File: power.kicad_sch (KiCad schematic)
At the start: 0 parts

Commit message: started on power
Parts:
- added C129, C131: 10n, Capacitor_SMD:C_0402_1005Metric, symbol Auto_Library_WUT:Kemet C0402C103K4PACTU
- added C130, C132: 10u, Capacitor_SMD:C_1206_3216Metric, symbol Auto_Library_WUT:Kyocera AVX 1206DD106MAT2A
- added C133, C134: 220p, Capacitor_SMD:C_0402_1005Metric, symbol Auto_Library_WUT:Kemet C0402C221G5GACTU
- added C135: 100n, Capacitor_SMD:C_0402_1005Metric, symbol Auto_Library_WUT:Yageo CC0402KRX7R8BB104
- added C136: 1u, Capacitor_SMD:C_0402_1005Metric, symbol Auto_Library_WUT:Kemet C0402C105K4PACTU
- added C137, C138, C141, C142: 47u, Capacitor_SMD:C_1206_3216Metric, symbol Auto_Library_WUT:TDK C3216X5R1E476M160AC
- added C139, C140: 10p, Capacitor_SMD:C_0402_1005Metric, symbol Auto_Library_WUT:Kemet C0402C100D4GACTU
- added L2, L3: 2u2, Inductor_WUT:Coilcraft_XEL4030, symbol Auto_Library_WUT:Coilcraft XEL4030-222MED
- added R64, R69, R71: 15k, Resistor_SMD:R_0402_1005Metric, symbol Auto_Library_WUT:KOA Speer RK73H1ETTP1502F
- added R65: 120k, Resistor_SMD:R_0402_1005Metric, symbol Auto_Library_WUT:KOA Speer RK73H1ETTP1203F
- added R66, R67: 10k, Resistor_SMD:R_0402_1005Metric, symbol Auto_Library_WUT:KOA Speer RK73H1ETTP1002F
- added R68, R70: 0R0, Resistor_SMD:R_0402_1005Metric, symbol Auto_Library_WUT:KOA Speer RK73Z1ETTP
- added R73: 300k, Resistor_SMD:R_0402_1005Metric, symbol Auto_Library_WUT:KOA Speer RK73H1ETTP3003F
- added R74: 56k, Resistor_SMD:R_0402_1005Metric, symbol Auto_Library_WUT:KOA Speer RK73H1ETTP5602F
- added R75: 470k, Resistor_SMD:R_0402_1005Metric, symbol Auto_Library_WUT:KOA Speer RK73H1ETTP4703F
- added R76: 150k, Resistor_SMD:R_0402_1005Metric, symbol Auto_Library_WUT:KOA Speer RK73H1ETTP1503F
- added R77: 100k, Resistor_SMD:R_0402_1005Metric, symbol Auto_Library_WUT:KOA Speer RK73H1ETTP1003F
- added R78, R79: 56m, Resistor_SMD:R_1020_2550Metric, symbol Auto_Library_WUT:Panasonic ERJB1CFR056U
- added U9: Analog LT8650SEV#PBF, IC_WUT:LQFN-32(28)-6EP_6x4mm_P0.5mm_EP1.1x1.33mm, symbol IC_WUT:LT8650SEV#PBF
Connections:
- new net: C137.1, C138.1, C139.1, L2.2, R73.1, R78.1
- new net: L2.1, U9.22 (SW1), U9.23 (SW1)
- new net: L3.1, U9.19 (SW2), U9.20 (SW2)
- new net: C140.1, C141.1, C142.1, L3.2, R75.1, R79.1
- new net: C133.1, R64.1
- new net: R71.1, U9.1 (RT)
- new net: R65.2, R66.1, U9.11 (EN1)
- new net: R68.2, R70.1, U9.16 (SYNC)
- new net: C136.1, R68.1, U9.25 (VCC)
- new net: R64.2, U9.27 (VC1)
- new net: C139.2, R73.2, R74.1, U9.28 (FB1)
- new net: C129.1, U9.29 (SS1)
- new net: C131.1, U9.30 (SS2)
- new net: C140.2, R75.2, R76.1, U9.31 (FB2)
- new net: R69.2, U9.32 (VC2)
- new net: C130.1, C132.1, R65.1, U9.4 (VIN1), U9.5 (VIN1), U9.7 (VIN2), U9.8 (VIN2)
- new net: C134.1, R69.1
- new net 0V: C129.2, C130.2, C131.2, C132.2, C133.2, C134.2, C135.2, C136.2, C137.2, C138.2, C141.2, C142.2, R66.2, R67.2, R70.2, R71.2, R74.2, R76.2, U9.10 (GND), U9.2 (GND), U9.33 (GND), U9.34 (GND), U9.35 (GND), U9.36 (GND), U9.37 (GND), U9.38 (GND), U9.MNT
- new net 3V3_PCIE: R79.2
- new net 3V3_PCIE_EN: C135.1, R67.1, U9.12 (EN2)
- new net 3V3_PI: R77.1
- new net 5V0_PI: R78.2
- new net PCIE_PGOOD: R77.2, U9.15 (PG2)
- no-connect marks 0 -> 5
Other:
- note added: "Low: Burst Mode Float: FCM without SS High: FCM with SS"
- note added: "Place 1u next to pin 25"
- note added: "TODO INA3221"
- note added: "TODO power input"
- note added: "Vcm(max) = 164mA I(max) = 3A R_sense = 55mR P(max) = 3*3*0.055 = 0.5W"
- note added: "Ven = 0.77V Vin(min) = 0.77 * (1+120/10) = 10V"
- note added: "fsw = 2MHz"
- note removed: "lt8650s"

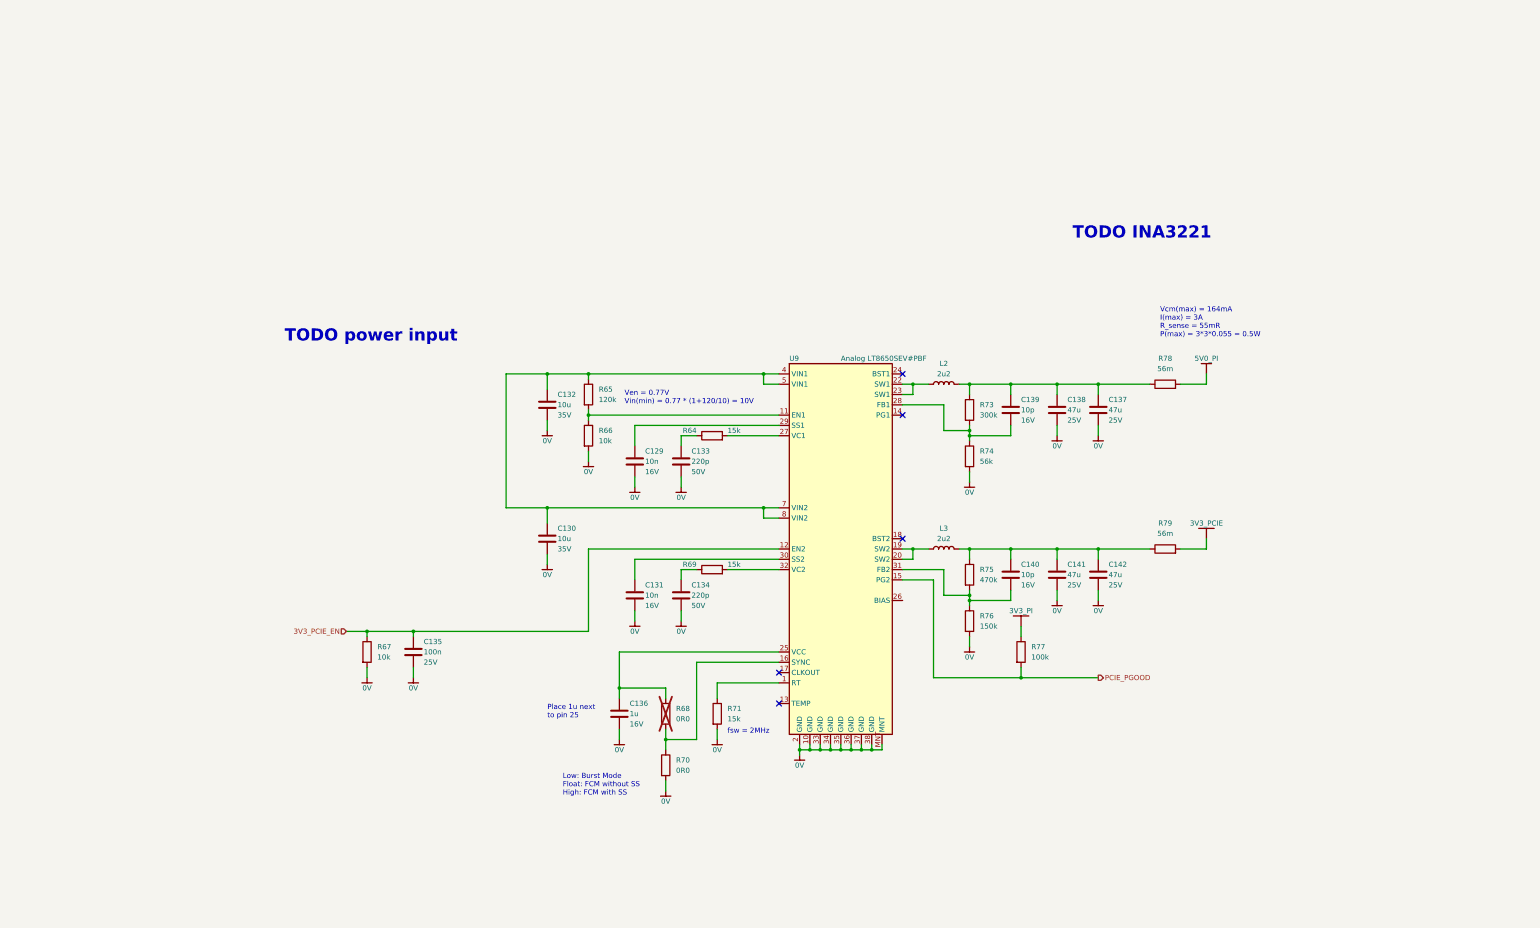
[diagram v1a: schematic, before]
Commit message: Added power supply
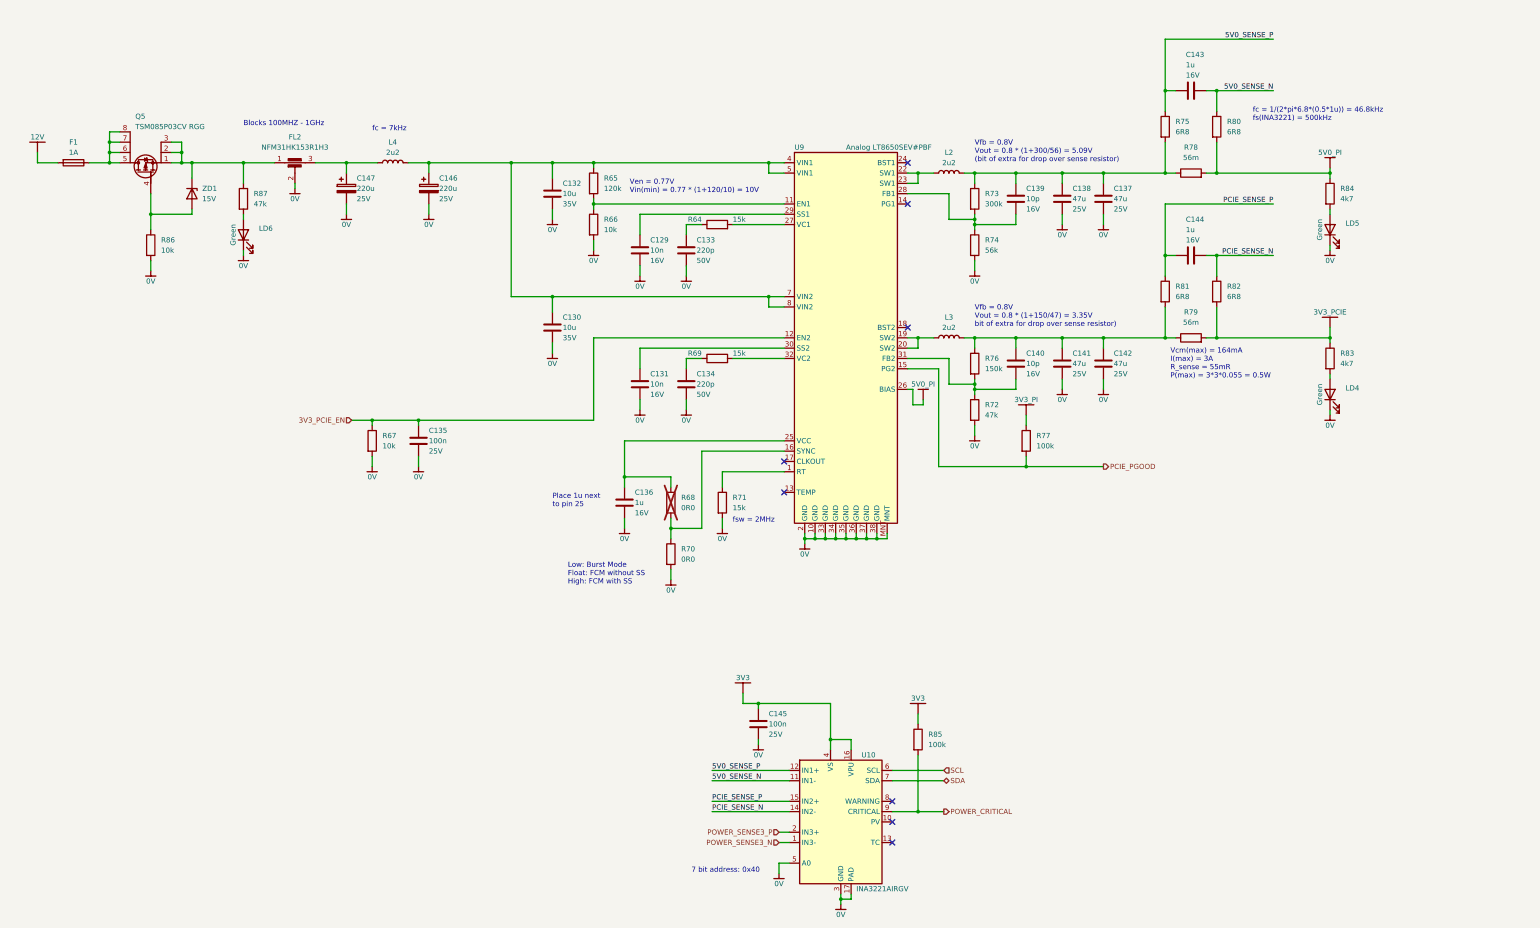
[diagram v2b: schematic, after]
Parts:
- removed R75: 470k, Resistor_SMD:R_0402_1005Metric, symbol Auto_Library_WUT:KOA Speer RK73H1ETTP4703F
- added C143, C144: 1u, Capacitor_SMD:C_0402_1005Metric, symbol Auto_Library_WUT:Kemet C0402C105K4PACTU
- added C145: 100n, Capacitor_SMD:C_0402_1005Metric, symbol Auto_Library_WUT:Yageo CC0402KRX7R8BB104
- added C146, C147: 220u, Capacitor_WUT:Wurth_WCAP-HSG5_8x10.5mm_SM, symbol Auto_Library_WUT:Wurth Elektronik_875575553004
- added F1: 1A, Fuse:Fuse_0603_1608Metric_Pad1.05x0.95mm_HandSolder, symbol Fuse_WUT:Littelfuse_0467001.NR
- added FL2: NFM31HK153R1H3, Capacitor_WUT:Murata_NFM31HK, symbol RF_WUT:Feedthrough_Murata_NFM31HK153R1H3
- added L4: 2u2, Inductor_WUT:Coilcraft_XEL4030, symbol Auto_Library_WUT:Coilcraft XEL4030-222MED
- added LD4, LD5, LD6: Green, LED_SMD:LED_0603_1608Metric, symbol Auto_Library_WUT:Ekinglux_E6C0603VGAC1UDA
- added Q5: TSM085P03CV RGG, IC_WUT:PDFN33-8, symbol FET_WUT:Taiwan_Semiconductor_TSM085P03CV-RGG_
- added R72, R87: 47k, Resistor_SMD:R_0402_1005Metric, symbol Auto_Library_WUT:KOA Speer RK73H1ETTP4702F
- added R75, R80, R81, R82: 6R8, Resistor_SMD:R_0402_1005Metric, symbol Auto_Library_WUT:KOA Speer RK73H1ETTP6R80F
- added R83, R84: 4k7, Resistor_SMD:R_0402_1005Metric, symbol Auto_Library_WUT:KOA Speer RK73H1ETTP4701F
- added R85: 100k, Resistor_SMD:R_0402_1005Metric, symbol Auto_Library_WUT:KOA Speer RK73H1ETTP1003F
- added R86: 10k, Resistor_SMD:R_0402_1005Metric, symbol Auto_Library_WUT:KOA Speer RK73H1ETTP1002F
- added U10: INA3221AIRGV, IC_WUT:Texas_VFQN-16-1EP_RGV0016A, symbol IC_WUT:INA3221AIRGV
- added ZD1: 15V, Diode_SMD:D_SOD-323, symbol Auto_Library_WUT:onsemi MM3Z15VST1G
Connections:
- net 0V: now also C145.2, C146.2, C147.2, FL2.2, LD4.1 (K), LD5.1 (K), LD6.1 (K), R72.2, R86.2, U10.17 (PAD), U10.3 (GND), U10.5 (A0); no longer R76.2
- net 3V3_PCIE: now also R82.2, R83.1
- net 5V0_PI: now also U9.26 (BIAS), R80.2, R84.1
- net at C137.1, C138.1, C139.1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: now also R75.2
- net at C140.1, C141.1, C142.1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: now also R76.1, R81.2
- net at C140.2, U9.31 (FB2): now also R76.2, R72.1; no longer R76.1
- net at C130.1, C132.1, R65.1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: now also C146.1, L4.2
- new net: FL2.1, Q5.1, Q5.2, Q5.3, R87.1, ZD1.1 (K)
- new net: Q5.4, R86.1, ZD1.2 (A)
- new net: F1.2, Q5.5, Q5.6, Q5.7, Q5.8
- new net: LD4.2 (A), R83.2
- new net: LD5.2 (A), R84.2
- new net: LD6.2 (A), R87.2
- new net: C147.1, FL2.3, L4.1
- new net 12V: F1.1
- new net 3V3: C145.1, R85.1, U10.16 (VPU), U10.4 (VS)
- new net 5V0_SENSE_N: C143.2, R80.1, U10.11 (IN1-)
- new net 5V0_SENSE_P: C143.1, R75.1, U10.12 (IN1+)
- new net PCIE_SENSE_N: C144.2, R82.1, U10.14 (IN2-)
- new net PCIE_SENSE_P: C144.1, R81.1, U10.15 (IN2+)
- new net POWER_CRITICAL: R85.2, U10.9 (CRITICAL)
- new net POWER_SENSE3_N: U10.1 (IN3-)
- new net POWER_SENSE3_P: U10.2 (IN3+)
- new net SCL: U10.6 (SCL)
- new net SDA: U10.7 (SDA)
- no-connect marks 5 -> 8
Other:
- note added: "7 bit address: 0x40"
- note added: "Blocks 100MHZ - 1GHz"
- note added: "Vfb = 0.8V Vout = 0.8 * (1+150/47) = 3.35V bit of extra for drop over sense resistor)"
- note added: "Vfb = 0.8V Vout = 0.8 * (1+300/56) = 5.09V (bit of extra for drop over sense resistor)"
- note added: "fc = 1/(2*pi*6.8*(0.5*1u)) = 46.8kHz fs(INA3221) = 500kHz"
- note added: "fc = 7kHz"
- note removed: "TODO INA3221"
- note removed: "TODO power input"
- moved on the sheet: C129, C130, C131, C132, C133, C134, C135, C136, C137, C138, C139, C140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

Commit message: Schematic mostly done
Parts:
- removed C144: 1u, Capacitor_SMD:C_0402_1005Metric, symbol Auto_Library_WUT:Kemet C0402C105K4PACTU
- removed R73: 300k, Resistor_SMD:R_0402_1005Metric, symbol Auto_Library_WUT:KOA Speer RK73H1ETTP3003F
- removed R74: 56k, Resistor_SMD:R_0402_1005Metric, symbol Auto_Library_WUT:KOA Speer RK73H1ETTP5602F
- removed R76: 150k, Resistor_SMD:R_0402_1005Metric, symbol Auto_Library_WUT:KOA Speer RK73H1ETTP1503F
- removed R81, R82: 6R8, Resistor_SMD:R_0402_1005Metric, symbol Auto_Library_WUT:KOA Speer RK73H1ETTP6R80F
- added C158: 1u, Capacitor_SMD:C_0402_1005Metric, symbol Auto_Library_WUT:Kemet C0402C105K4PACTU
- added R130, R131: 6R8, Resistor_SMD:R_0402_1005Metric, symbol Auto_Library_WUT:KOA Speer RK73H1ETTP6R80F
- added R73: 160k, Resistor_SMD:R_0402_1005Metric, symbol Auto_Library_WUT:KOA Speer RK73H1ETTP1603F
- added R74: 30k, Resistor_SMD:R_0402_1005Metric, symbol Auto_Library_WUT:KOA Speer RK73H1ETTP3002F
- added R76: 15k, Resistor_SMD:R_0402_1005Metric, symbol Auto_Library_WUT:KOA Speer RK73H1ETTP1502F
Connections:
- net 3V3_PI is gone; now on net 3V3: R77.1
- net 0V: now also R74.2, R76.2; no longer R72.2
- net 3V3_PCIE: now also C140.1, R72.1, R80.1
- net 5V0_PI: now also C139.1, R131.1, R73.1; no longer R80.2
- net 5V0_SENSE_N: now also C158.2, R131.2; no longer C143.2, R80.1
- net 5V0_SENSE_P: now also C158.1, R130.2; no longer C143.1, R75.1
- net PCIE_SENSE_N: now also C143.2, R80.2
- net PCIE_SENSE_P: now also C143.1, R75.2
- net at C137.1, C138.1, L2.2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: now also R130.1; no longer C139.1, R75.2
- net at C141.1, C142.1, L3.2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: now also R75.1; no longer C140.1
- net at C139.2, U9.28 (FB1): now also R73.2, R74.1
- net at C140.2, U9.31 (FB2): now also R72.2, R76.1; no longer R72.1
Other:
- note added: "Vfb = 0.8V Vout = 0.8 * (1+300/56) = 5.09V"
- note added: "Vfb = 0.8V Vout = 0.8 * (1+47/15) = 3.31V"
- note removed: "Vfb = 0.8V Vout = 0.8 * (1+150/47) = 3.35V bit of extra for drop over sense resistor)"
- note removed: "Vfb = 0.8V Vout = 0.8 * (1+300/56) = 5.09V (bit of extra for drop over sense resistor)"
- moved on the sheet: C137, C138, C141, C142, LD4, LD5, R77, R78, R79, R83, R84

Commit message: schematic complete
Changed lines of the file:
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@@
   (junction (at 299.72 58.42) (diameter 0) (color 0 0 0 0)
+  )
+  (junction (at 121.92 55.88) (diameter 0) (color 0 0 0 0)
   )
   (junction (at 104.14 119.38) (diameter 0) (color 0 0 0 0)
@@
     (stroke (width 0) (type default))
   )
-  (wire (pts (xy 118.11 55.88) (xy 138.43 55.88))
+  (wire (pts (xy 118.11 55.88) (xy 121.92 55.88))
     (stroke (width 0) (type default))
   )
@@
   )
   (wire (pts (xy 287.02 58.42) (xy 289.56 58.42))
+    (stroke (width 0) (type default))
+  )
+  (wire (pts (xy 121.92 55.88) (xy 138.43 55.88))
     (stroke (width 0) (type default))
   )
@@
         )
       )
+    )
+  )
+  (symbol (lib_id "Power_WUT:PWR_FLAG") (at 121.92 55.88 0) (unit 1)
+    (in_bom yes) (on_board yes) (dnp no) (fields_autoplaced)
+    (property "Reference" "#FLG033" (at 121.92 53.975 0)
+      (effects (font (size 1.27 1.27)) hide)
+    )
+    (property "Value" "PWR_FLAG" (at 121.92 52.07 0)
+      (effects (font (size 1.27 1.27)) hide)
+    )
+    (property "Footprint" "" (at 121.92 55.88 0)
+      (effects (font (size 1.27 1.27)) hide)
+    )
+    (property "Datasheet" "~" (at 121.92 55.88 0)
+      (effects (font (size 1.27 1.27)) hide)
+    )
+    (pin "1")
+    (instances
+      (project "Master Timing Card"
+        (path "/6e8e281e-e30f-459d-852f-231836068db5/d6642cbe-acae-4c5e-b434-aaa25d469dab"
+          (reference "#FLG033") (unit 1)
+        )
+      )

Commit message: Moved to preferred library
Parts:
- C135, C145: symbol Auto_Library_WUT:Yageo CC0402KRX7R8BB104 -> Preferred_WUT:Yageo CC0402KRX7R8BB104
- LD4, LD5, LD6: symbol Auto_Library_WUT:Ekinglux_E6C0603VGAC1UDA -> Preferred_WUT:Ekinglux_E6C0603VGAC1UDA
- R66, R67, R86: symbol Auto_Library_WUT:KOA Speer RK73H1ETTP1002F -> Preferred_WUT:KOA Speer RK73H1ETTP1002F
- R68, R70: symbol Auto_Library_WUT:KOA Speer RK73Z1ETTP -> Preferred_WUT:KOA Speer RK73Z1ETTP
- R77, R85: symbol Auto_Library_WUT:KOA Speer RK73H1ETTP1003F -> Preferred_WUT:KOA Speer RK73H1ETTP1003F
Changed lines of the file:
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@@
     (effects (font (size 1.27 1.27)) (justify right))
   )
-  (symbol (lib_id "Auto_Library_WUT:KOA Speer RK73H1ETTP1003F") (at 266.7 134.62 0) (unit 1)
+  (symbol (lib_id "Preferred_WUT:KOA Speer RK73H1ETTP1003F") (at 266.7 134.62 0) (unit 1)
     (in_bom yes) (on_board yes) (dnp no)
     (property "Reference" "R77" (at 269.24 133.35 0)
@@
     )
   )
-  (symbol (lib_id "Auto_Library_WUT:KOA Speer RK73H1ETTP1002F") (at 104.14 124.46 0) (unit 1)
+  (symbol (lib_id "Preferred_WUT:KOA Speer RK73H1ETTP1002F") (at 104.14 124.46 0) (unit 1)
     (in_bom yes) (on_board yes) (dnp no) (fields_autoplaced)
     (property "Reference" "R67" (at 106.68 123.19 0)
@@
     )
   )
-  (symbol (lib_id "Auto_Library_WUT:Ekinglux_E6C0603VGAC1UDA") (at 327.66 72.39 270) (unit 1)
+  (symbol (lib_id "Preferred_WUT:Ekinglux_E6C0603VGAC1UDA") (at 327.66 72.39 270) (unit 1)
     (in_bom yes) (on_board yes) (dnp no) (fields_autoplaced)
     (property "Reference" "LD5" (at 331.47 70.8025 90)
@@
     )
   )
-  (symbol (lib_id "Auto_Library_WUT:Ekinglux_E6C0603VGAC1UDA") (at 72.39 73.66 270) (unit 1)
+  (symbol (lib_id "Preferred_WUT:Ekinglux_E6C0603VGAC1UDA") (at 72.39 73.66 270) (unit 1)
     (in_bom yes) (on_board yes) (dnp no) (fields_autoplaced)
     (property "Reference" "LD6" (at 76.2 72.0725 90)
@@
     )
   )
-  (symbol (lib_id "Auto_Library_WUT:Yageo CC0402KRX7R8BB104") (at 199.39 194.31 0) (unit 1)
+  (symbol (lib_id "Preferred_WUT:Yageo CC0402KRX7R8BB104") (at 199.39 194.31 0) (unit 1)
     (in_bom yes) (on_board yes) (dnp no) (fields_autoplaced)
     (property "Reference" "C145" (at 201.93 191.77 0) (do_not_autoplace)
@@
     )
   )
-  (symbol (lib_id "Auto_Library_WUT:KOA Speer RK73Z1ETTP") (at 177.8 152.4 0) (unit 1)
+  (symbol (lib_id "Preferred_WUT:KOA Speer RK73Z1ETTP") (at 177.8 152.4 0) (unit 1)
     (in_bom yes) (on_board yes) (dnp no) (fields_autoplaced)
     (property "Reference" "R70" (at 180.34 151.13 0)
@@
     )
   )
-  (symbol (lib_id "Auto_Library_WUT:KOA Speer RK73H1ETTP1002F") (at 49.53 76.2 0) (unit 1)
+  (symbol (lib_id "Preferred_WUT:KOA Speer RK73H1ETTP1002F") (at 49.53 76.2 0) (unit 1)
     (in_bom yes) (on_board yes) (dnp no) (fields_autoplaced)
     (property "Reference" "R86" (at 52.07 74.93 0)
@@
     )
   )
-  (symbol (lib_id "Auto_Library_WUT:KOA Speer RK73Z1ETTP") (at 177.8 139.7 0) (unit 1)
+  (symbol (lib_id "Preferred_WUT:KOA Speer RK73Z1ETTP") (at 177.8 139.7 0) (unit 1)
     (in_bom yes) (on_board yes) (dnp yes) (fields_autoplaced)
     (property "Reference" "R68" (at 180.34 138.43 0)
@@
     )
   )
-  (symbol (lib_id "Auto_Library_WUT:KOA Speer RK73H1ETTP1002F") (at 158.75 71.12 0) (unit 1)
+  (symbol (lib_id "Preferred_WUT:KOA Speer RK73H1ETTP1002F") (at 158.75 71.12 0) (unit 1)
     (in_bom yes) (on_board yes) (dnp no) (fields_autoplaced)
     (property "Reference" "R66" (at 161.29 69.85 0)
@@
     )
   )
-  (symbol (lib_id "Auto_Library_WUT:Yageo CC0402KRX7R8BB104") (at 115.57 124.46 0) (unit 1)
+  (symbol (lib_id "Preferred_WUT:Yageo CC0402KRX7R8BB104") (at 115.57 124.46 0) (unit 1)
     (in_bom yes) (on_board yes) (dnp no) (fields_autoplaced)
     (property "Reference" "C135" (at 118.11 121.92 0) (do_not_autoplace)
@@
     )
   )
-  (symbol (lib_id "Auto_Library_WUT:Ekinglux_E6C0603VGAC1UDA") (at 327.66 113.03 270) (unit 1)
+  (symbol (lib_id "Preferred_WUT:Ekinglux_E6C0603VGAC1UDA") (at 327.66 113.03 270) (unit 1)
     (in_bom yes) (on_board yes) (dnp no) (fields_autoplaced)
     (property "Reference" "LD4" (at 331.47 111.4425 90)
@@
     )
   )
-  (symbol (lib_id "Auto_Library_WUT:KOA Speer RK73H1ETTP1003F") (at 238.76 198.12 0) (unit 1)
+  (symbol (lib_id "Preferred_WUT:KOA Speer RK73H1ETTP1003F") (at 238.76 198.12 0) (unit 1)
     (in_bom yes) (on_board yes) (dnp no) (fields_autoplaced)
     (property "Reference" "R85" (at 241.3 196.85 0)

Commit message: Started placement
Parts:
- U10: footprint IC_WUT:Texas_VFQN-16-1EP_RGV0016A -> IC_WUT:Texas_VQFN-16-1EP_RGV0016A
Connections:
- net 5V0_PI: no longer U9.26 (BIAS)
- net 12V_PROT: now reaches FL2.1, Q5.1, Q5.2, Q5.3, R87.1, ZD1.1 (K)
- net 12V_F: now reaches F1.2, Q5.5, Q5.6, Q5.7, Q5.8
- net SW1: now reaches L2.1, U9.22 (SW1), U9.23 (SW1)
- net SW2: now reaches L3.1, U9.19 (SW2), U9.20 (SW2)
- net 12V_DCDC: now reaches C130.1, C132.1, C146.1, L4.2, R65.1, U9.4 (VIN1), U9.5 (VIN1), U9.7 (VIN2), U9.8 (VIN2)
- net 12V_FILT: now reaches C147.1, FL2.3, L4.1
- no-connect marks 8 -> 9
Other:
- moved on the sheet: F1, L2, L3

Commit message: layout progress
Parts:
- C146: renamed from C135; symbol Preferred_WUT:Yageo CC0402KRX7R8BB104 -> AAA_Preferred_WUT:Yageo CC0402KRX7R8BB104
- C155: renamed from C145; symbol Preferred_WUT:Yageo CC0402KRX7R8BB104 -> AAA_Preferred_WUT:Yageo CC0402KRX7R8BB104
- LD7: renamed from LD6; symbol Preferred_WUT:Ekinglux_E6C0603VGAC1UDA -> AAA_Preferred_WUT:Ekinglux_E6C0603VGAC1UDA
- LD8: renamed from LD5; symbol Preferred_WUT:Ekinglux_E6C0603VGAC1UDA -> AAA_Preferred_WUT:Ekinglux_E6C0603VGAC1UDA
- LD9: renamed from LD4; symbol Preferred_WUT:Ekinglux_E6C0603VGAC1UDA -> AAA_Preferred_WUT:Ekinglux_E6C0603VGAC1UDA
- Q6: renamed from Q5; symbol FET_WUT:Taiwan_Semiconductor_TSM085P03CV-RGG_ -> Transistor_WUT:Taiwan-Semiconductor_TSM085P03CV-RGG
- R101: renamed from R86; symbol Preferred_WUT:KOA Speer RK73H1ETTP1002F -> AAA_Preferred_WUT:KOA Speer RK73H1ETTP1002F
- R103: renamed from R67; symbol Preferred_WUT:KOA Speer RK73H1ETTP1002F -> AAA_Preferred_WUT:KOA Speer RK73H1ETTP1002F
- R105: renamed from R66; symbol Preferred_WUT:KOA Speer RK73H1ETTP1002F -> AAA_Preferred_WUT:KOA Speer RK73H1ETTP1002F
- R106: renamed from R68; symbol Preferred_WUT:KOA Speer RK73Z1ETTP -> AAA_Preferred_WUT:KOA Speer RK73Z1ETTP
- R107: renamed from R70; symbol Preferred_WUT:KOA Speer RK73Z1ETTP -> AAA_Preferred_WUT:KOA Speer RK73Z1ETTP
- R111: renamed from R85; symbol Preferred_WUT:KOA Speer RK73H1ETTP1003F -> AAA_Preferred_WUT:KOA Speer RK73H1ETTP1003F
- R112: renamed from R77; symbol Preferred_WUT:KOA Speer RK73H1ETTP1003F -> AAA_Preferred_WUT:KOA Speer RK73H1ETTP1003F
- renumbered C147 to C145, C146 to C147, C132 to C148, C130 to C149, C136 to C150, C129 to C151, C131 to C152, C133 to C153, C134 to C154, C138 to C156, C141 to C157, C137 to C158, C142 to C159, C139 to C160, C140 to C161, C158 to C162, C143 to C163, FL2 to FL3, L4 to L6, L2 to L7, L3 to L8, R87 to R102, R65 to R104, R64 to R108, R69 to R109, R71 to R110, R78 to R113, R79 to R114, R73 to R115, R74 to R116, R72 to R117, R76 to R118, R84 to R119, R83 to R120, R130 to R121, R131 to R122, R75 to R123, R80 to R124, U10 to U17, U9 to U18
